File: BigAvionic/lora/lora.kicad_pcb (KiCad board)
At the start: 2 copper layers, 68 x 68 mm, 14 parts, among them U10 E22-400T30S, U11 E80-900M23313S

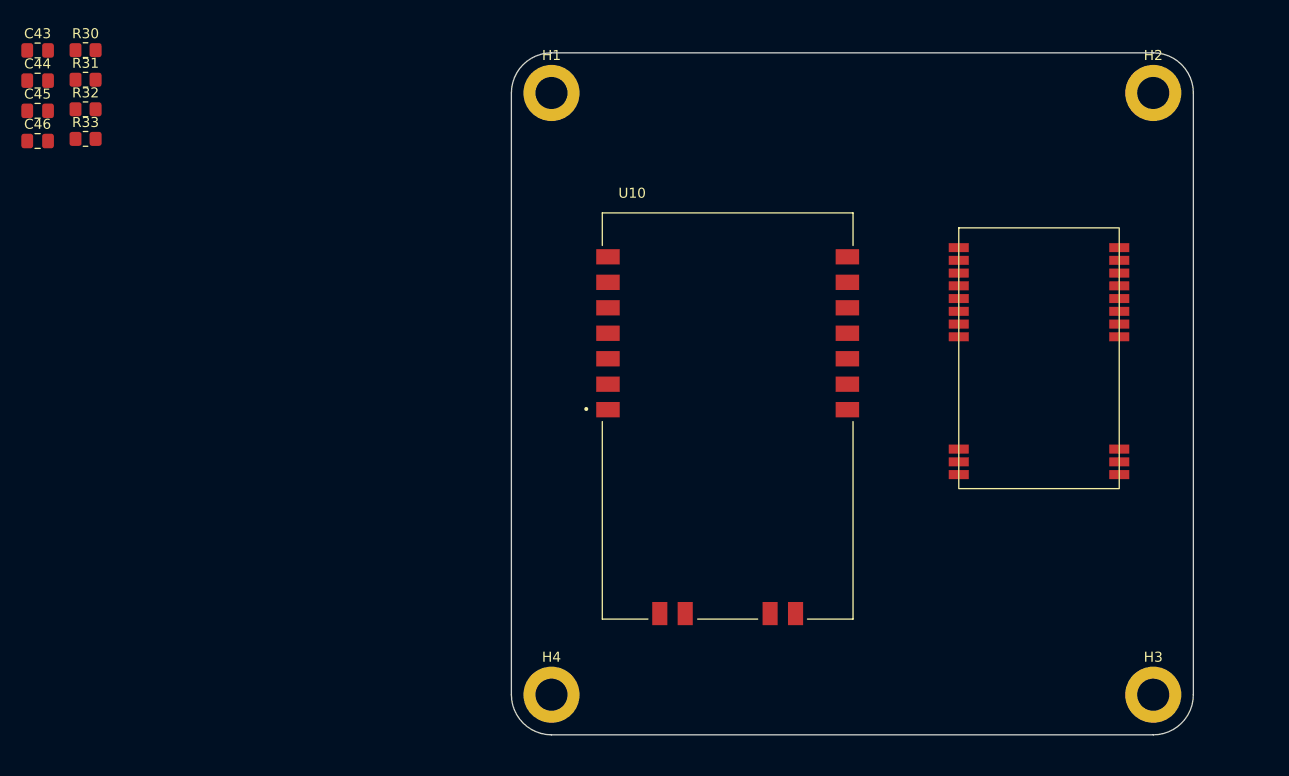
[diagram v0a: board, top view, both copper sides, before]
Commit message: finish lora layer
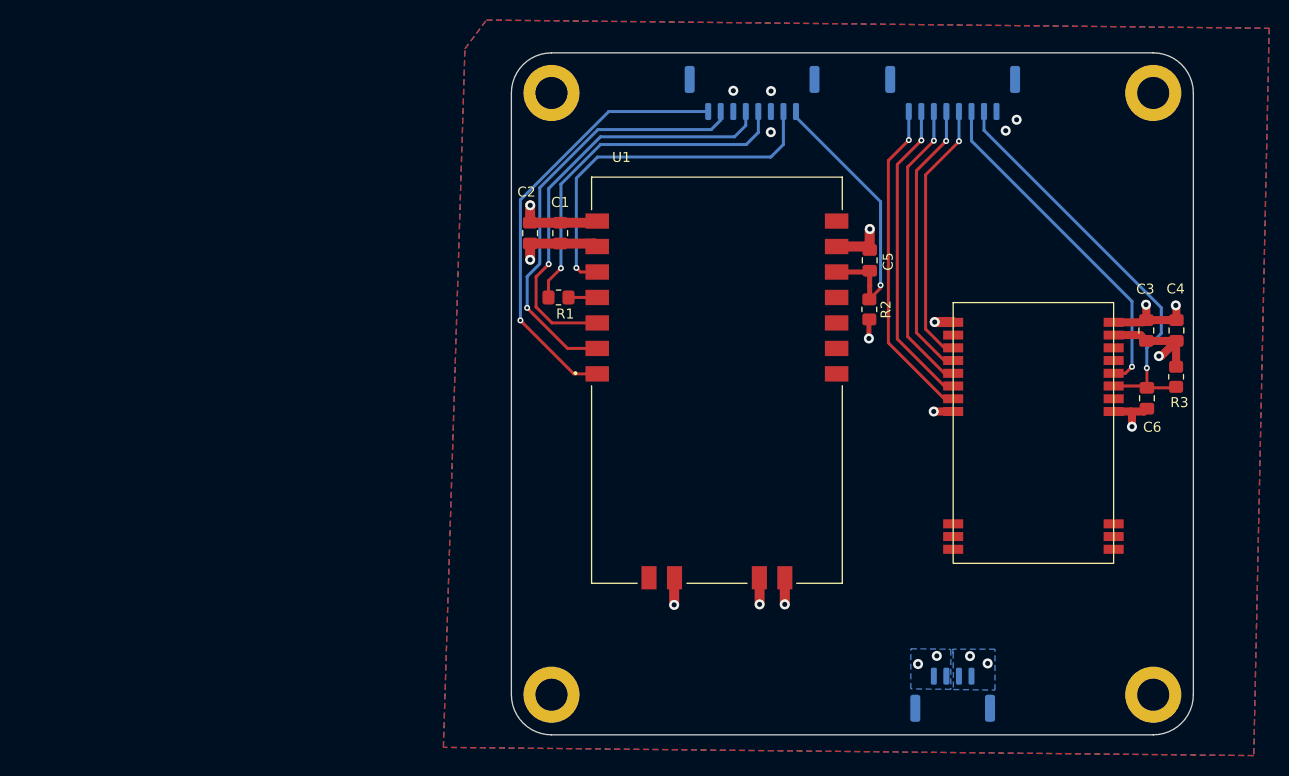
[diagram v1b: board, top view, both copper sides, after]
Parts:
- removed R30: 22ohm, Resistor_SMD:R_0805_2012Metric_Pad1.20x1.40mm_HandSolder
- added C5: 100n, Capacitor_SMD:C_0805_2012Metric_Pad1.18x1.45mm_HandSolder, F.Cu at (155.0, 77.9)
- added C6: 100n, Capacitor_SMD:C_0805_2012Metric_Pad1.18x1.45mm_HandSolder, F.Cu at (182.6, 91.6)
- added J1: Conn_01x04, Connector_JST:JST_GH_SM04B-GHS-TB_1x04-1MP_P1.25mm_Horizontal, B.Cu at (163.2, 121.2)
- added J2: Conn_01x08, Connector_JST:JST_GH_SM08B-GHS-TB_1x08-1MP_P1.25mm_Horizontal, B.Cu at (143.2, 61.2)
- added J3: Conn_01x08, Connector_JST:JST_GH_SM08B-GHS-TB_1x08-1MP_P1.25mm_Horizontal, B.Cu at (163.2, 61.2)
- moved C4 115.1 mm to (185.6, 84.9), turned to 90 degrees
- moved C3 112.7 mm to (182.6, 84.9), turned to 90 degrees
- moved R3 111.3 mm to (185.5, 89.5), turned to 90 degrees
- moved R2 80.7 mm to (154.9, 82.8), turned to -90 degrees
- moved C1 55.2 mm to (124.1, 75.2), turned to 90 degrees
- moved R1 51.9 mm to (123.9, 81.6), turned to 180 degrees
- moved C2 51.4 mm to (121.1, 75.2), turned to 90 degrees
- moved U2 7.47 mm to (171.3, 95.1)
- moved U1 3.73 mm to (139.7, 89.8)
- renumbered C43 to C1, C44 to C2, C45 to C3, C46 to C4, R31 to R1, R32 to R2, R33 to R3, U10 to U1, U11 to U2
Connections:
- U1 pad 5: Net-(U10-RXD) -> UART3_TX
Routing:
- net LORA433_M0: track 0.00 -> 44.6 mm, vias 0 -> 1
- net LORA433_M1: track 0.00 -> 43.2 mm, vias 0 -> 1
- net UART3_TX: track 0.00 -> 42.7 mm, vias 0 -> 1
- net GND: track 0.00 -> 42.3 mm, vias 0 -> 17
- net LORA920_RST: track 0.00 -> 41.8 mm, vias 0 -> 1
- net LORA433_BUSY: track 0.00 -> 36.3 mm, vias 0 -> 1
- net UART3_RX: track 0.00 -> 35.7 mm, vias 0 -> 1
- net LORA920_INT: track 0.00 -> 34.2 mm, vias 0 -> 1
- net LORA920_BUSY: track 0.00 -> 32.7 mm, vias 0 -> 1
- net CSB_LORA920: track 0.00 -> 31.2 mm, vias 0 -> 1
- net SPI3_SCK: track 0.00 -> 29.6 mm, vias 0 -> 1
- net LORA433_RST: track 0.00 -> 29.0 mm, vias 0 -> 1
- net SPI3_MOSI: track 0.00 -> 28.1 mm, vias 0 -> 1
- net SPI3_MISO: track 0.00 -> 26.6 mm, vias 0 -> 1
- net +3.3V: track 0.00 -> 22.0 mm, vias 0 -> 5
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- added copper zone on B.Cu, net +3.3V
- added copper zone on In2.Cu, net +3.3V
- added copper zone on B.Cu, net GND
- added copper zone on F.Cu, net GND
- added copper zone on In1.Cu, net GND
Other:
- copper layers 2 -> 4

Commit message: finish lora & top
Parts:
- added 3V3: TestPoint, TestPoint:TestPoint_Pad_D1.0mm, F.Cu at (166.0, 113.9)
- added D1: RED_LED, LED_SMD:LED_0805_2012Metric_Pad1.15x1.40mm_HandSolder, F.Cu at (175.2, 117.2)
- added GND1: TestPoint, TestPoint:TestPoint_Pad_D1.0mm, F.Cu at (161.3, 113.9)
- added R4: 1k, Resistor_SMD:R_0805_2012Metric_Pad1.20x1.40mm_HandSolder, F.Cu at (170.7, 117.2)
- renumbered C5 to C3, C3 to C4, C4 to C5
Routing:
- net +3.3V: track 22.0 -> 29.3 mm
- net GND: track 42.3 -> 45.9 mm, vias 17 -> 240
- net Net-(D1-A): track 0.00 -> 2.48 mm

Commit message: power layer finished
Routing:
- net GND: track 45.9 -> 42.9 mm
- net +3.3V: vias 5 -> 6

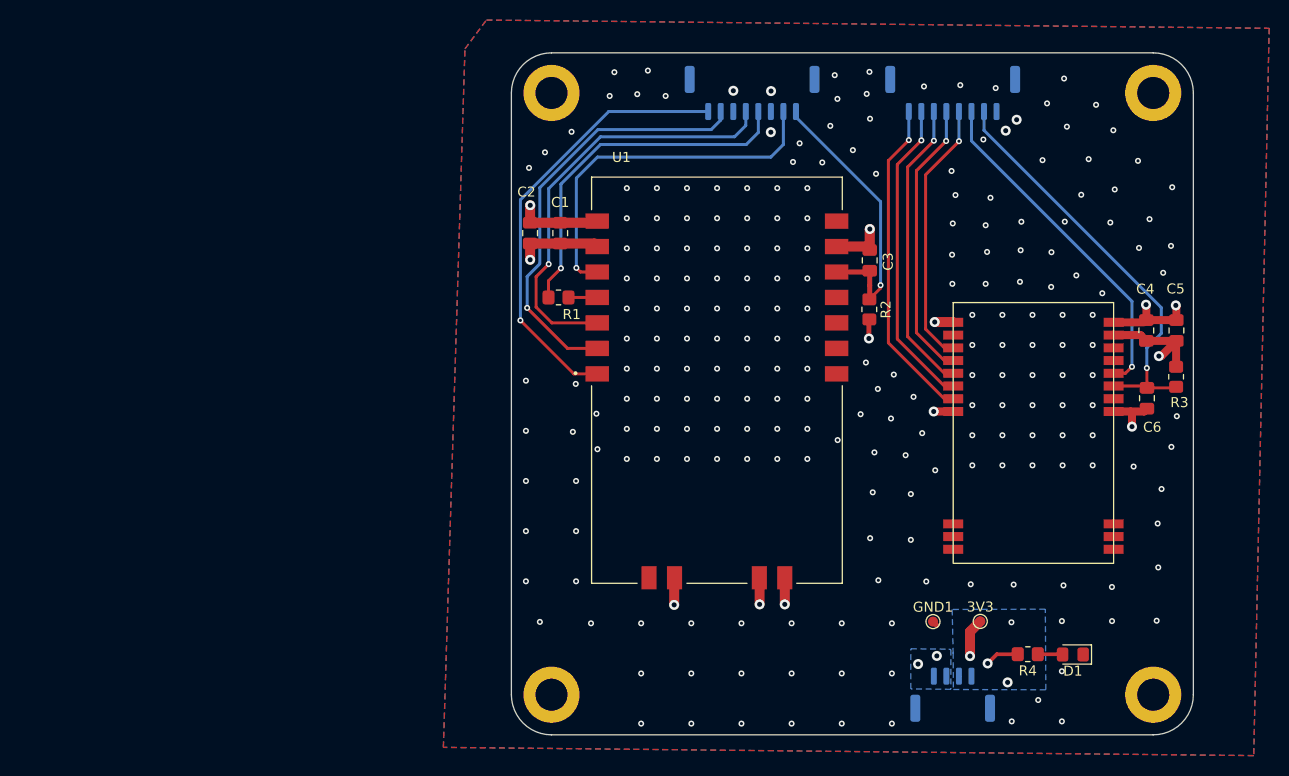
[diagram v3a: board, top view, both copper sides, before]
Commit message: check lora top power generate garber
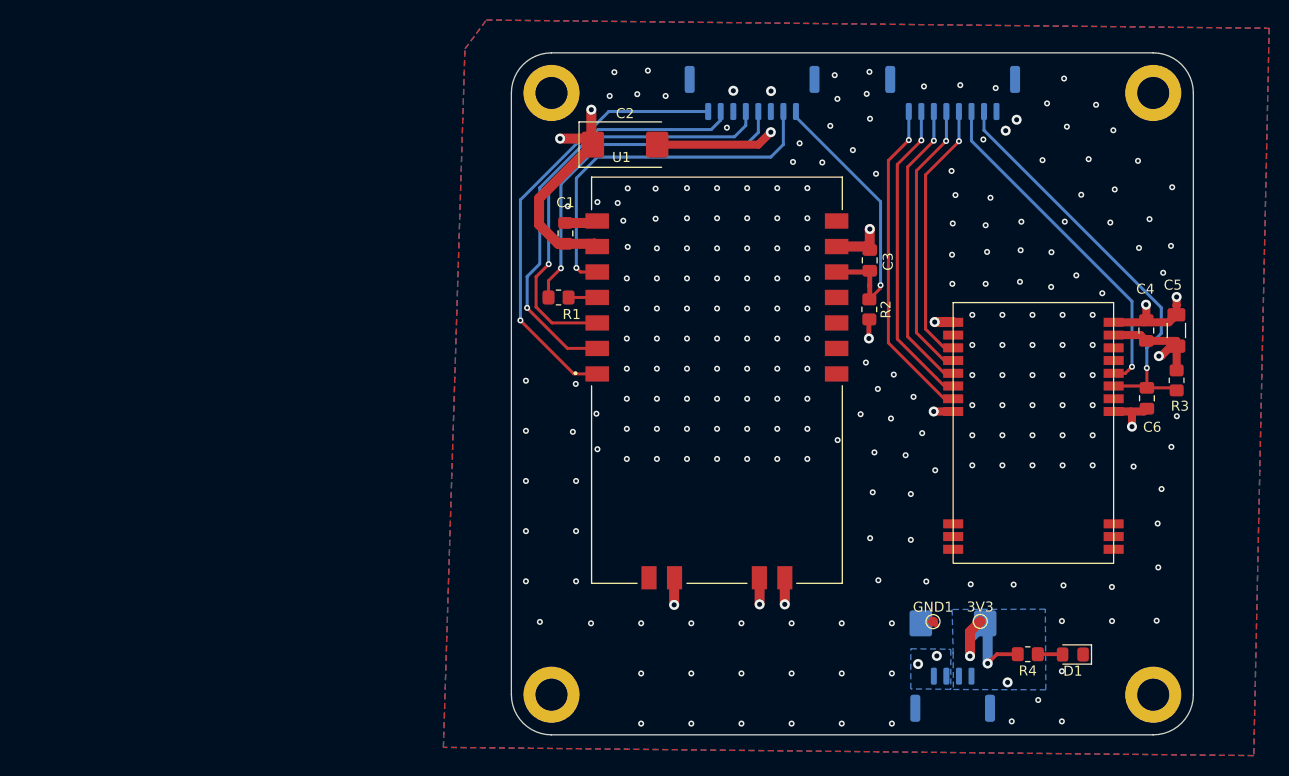
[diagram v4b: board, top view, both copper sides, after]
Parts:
- added C7: 470u, Capacitor_Tantalum_SMD:CP_EIA-7343-43_Kemet-X_HandSolder, B.Cu at (163.3, 114.1)
- C2: footprint Capacitor_SMD:C_0805_2012Metric_Pad1.18x1.45mm_HandSolder -> Capacitor_Tantalum_SMD:CP_EIA-7343-31_Kemet-D_HandSolder
- C5: footprint Capacitor_SMD:C_0805_2012Metric_Pad1.18x1.45mm_HandSolder -> Capacitor_SMD:C_1206_3216Metric_Pad1.33x1.80mm_HandSolder
- moved C2 12.9 mm to (130.6, 66.3), turned to 0 degrees
- moved C1 0.52 mm to (124.6, 75.2)
- moved R3 0.36 mm to (185.6, 89.9)
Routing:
- net +3.3V: track 29.3 -> 53.6 mm, vias 6 -> 7
- net GND: track 42.9 -> 49.4 mm, vias 240 -> 239

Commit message: MCU process
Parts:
- moved D1 20.6 mm to (154.9, 120.8), turned to 90 degrees
- moved R4 15.9 mm to (154.9, 115.2), turned to 90 degrees
- moved 3V3 10.1 mm to (156.2, 111.6)
- moved GND1 9.48 mm to (170.7, 113.1)
- turned C7 to 180 degrees
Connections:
- J1 pad 1: +3.3V -> GND
- J1 pad 2: +3.3V -> GND
- J1 pad 3: GND -> +3.3V
- J1 pad 4: GND -> +3.3V
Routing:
- net +3.3V: track 53.6 -> 43.5 mm, vias 7 -> 8
- net GND: track 49.4 -> 56.9 mm, vias 239 -> 240
- net Net-(D1-A): track 2.48 -> 3.55 mm
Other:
- board text added: "LORA Layer v1"
- board text added: "S_L433"
- board text added: "S_L920"

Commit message: MCU layer progress 1
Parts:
- added D2: TVS, Diode_SMD:D_SMA, B.Cu at (153.6, 117.2)

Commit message: version for v1 production
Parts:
- added G***: LOGO, Lib:LOGO-10*12.1, F.Cu at (165.2, 75.1)
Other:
- board text added: "3V3"
- board text added: "GND"
- board text added: "NCKU Ius Bubulae Avionics v1.0 Tony"
